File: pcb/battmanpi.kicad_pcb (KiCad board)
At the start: 2 copper layers, 65 x 56 mm, 80 parts, among them CON1 CHARGE PSU, K1 TX2-5V, K2 TX2-5V, P1 SEN+, P2 SEN-, P3 BAT+, P4 BAT-, P5 Raspberry Pi, P6 FAN, Q1 2N3904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

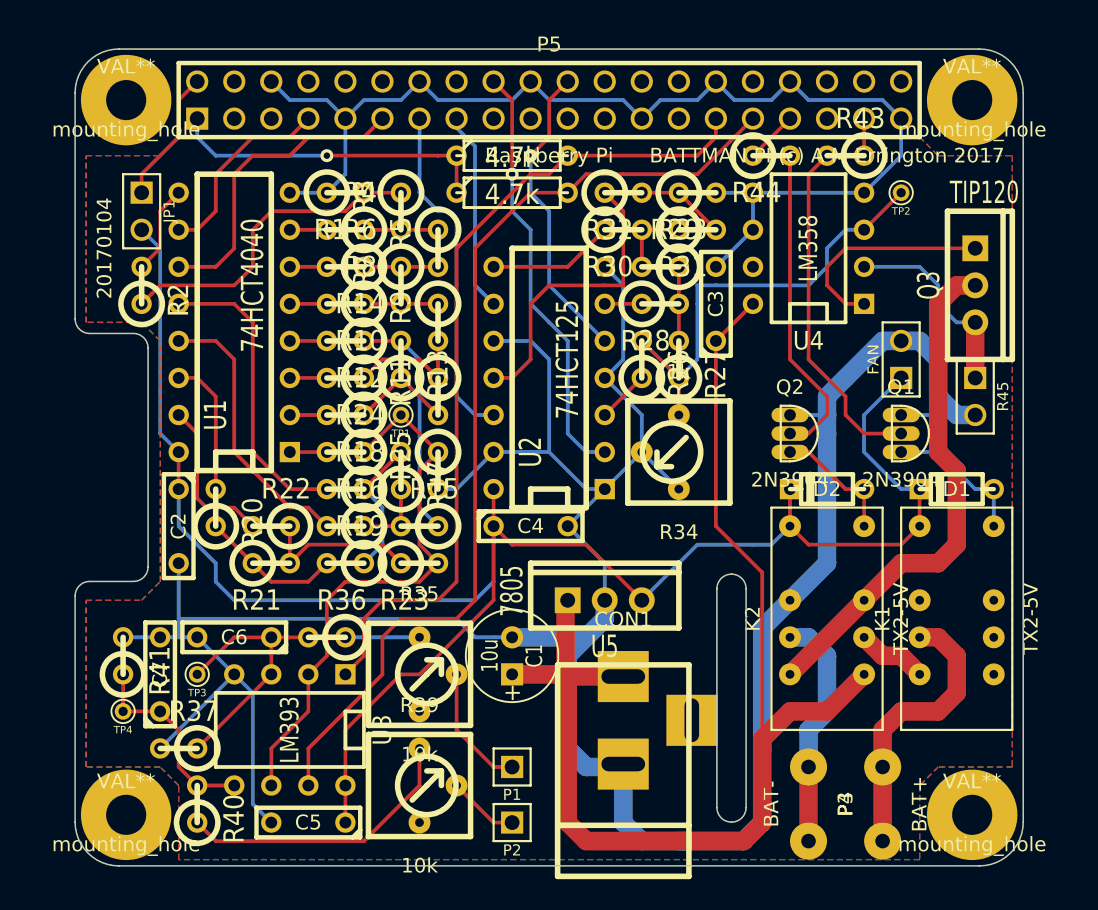
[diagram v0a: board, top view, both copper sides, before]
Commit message: Almost final PCB layout.  All holes set to 0.8 or 1.0 mm (except special components and mounting).  Next make traces slightly wider.
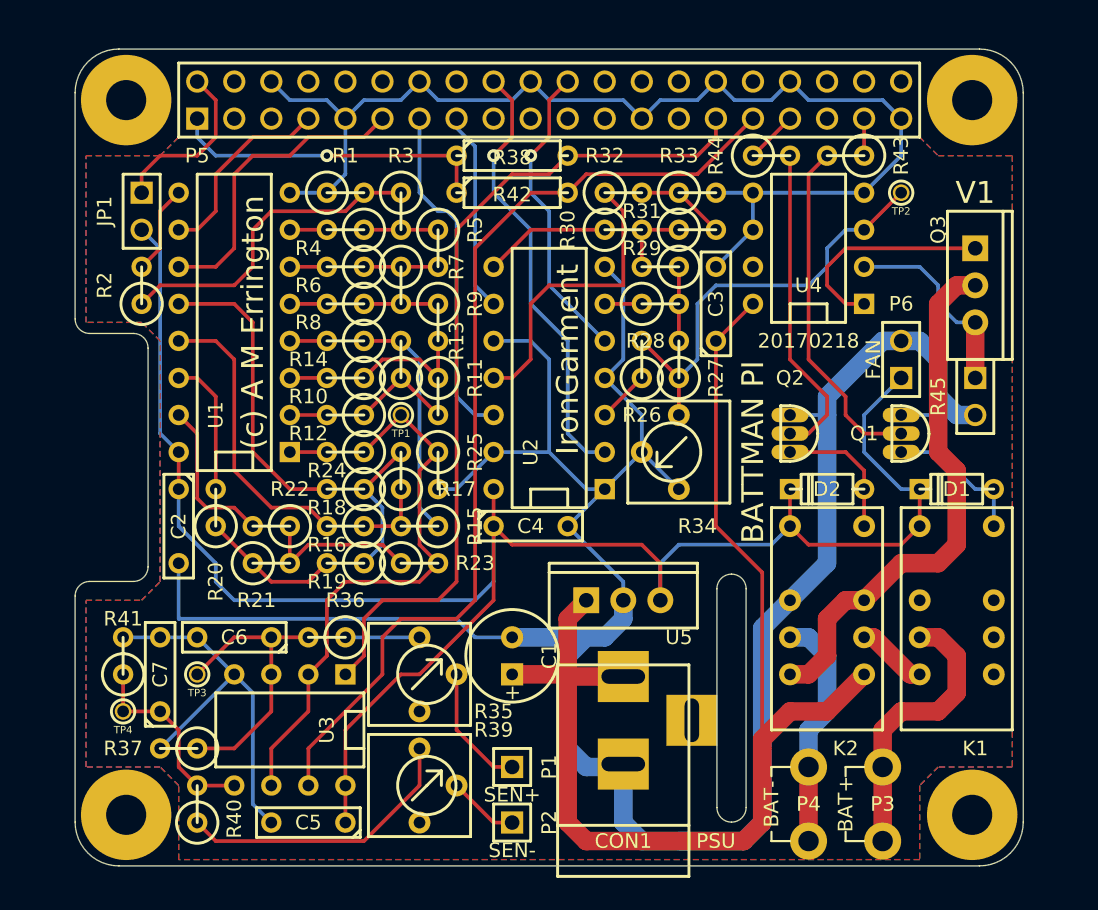
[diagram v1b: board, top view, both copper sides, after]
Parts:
- CON1: value CHARGE PSU -> PSU
- moved U5 1.27 mm to (133.3, 101.6)
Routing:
- net +5V: track 128.5 -> 131.5 mm
- net N-0000067: track 9.20 -> 11.7 mm
- net N-0000032: track 35.2 -> 36.7 mm
- net N-0000030: track 18.4 -> 19.9 mm
- net /D3: track 29.3 -> 30.4 mm
- net /VDAC<B+: track 56.8 -> 57.5 mm
- net N-0000031: track 8.67 -> 9.42 mm
- net N-0000013: track 19.1 -> 19.9 mm
- net N-0000079: track 30.4 -> 29.6 mm
- net +24V: track 84.6 -> 85.1 mm
- net GND: track 281.2 -> 281.8 mm
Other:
- board text added: "(c) A M Errington"
- board text added: "20170218"
- board text added: "BATTMAN PI"
- board text added: "IronGarment"
- board text added: "V1"
- board text removed: "20170104"
- board text removed: "BATTMAN PI (c) A M Errington 2017"

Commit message: Latest KiCad project files
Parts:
- moved R43 14.5 mm to (144.8, 85.1), turned to 270 degrees
- moved R44 14.0 mm to (142.2, 85.1), turned to 270 degrees
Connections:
- P5 pad 13: /D0 -> (no net)
- P5 pad 15: /D1 -> /D0
- P5 pad 16: (no net) -> /D1
- P5 pad 4: (no net) -> N-0000067
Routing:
- net GND: track 281.8 -> 314.5 mm, vias 0 -> 1
- net N-0000030: track 21.9 -> 5.61 mm
- net /CNCT: track 2.54 -> 17.3 mm
- net N-0000027: track 23.7 -> 9.20 mm
- net /MODE: track 3.59 -> 16.3 mm
- net N-0000081: track 15.0 -> 9.20 mm
- net +5V: track 131.5 -> 135.1 mm
- net /D1: track 13.8 -> 17.3 mm
- net /ZERO: track 21.2 -> 18.2 mm
- net N-0000067: track 11.7 -> 13.5 mm
- net /INCR: track 13.5 -> 12.0 mm
- net /D0: track 23.5 -> 22.4 mm
- net /D3: track 30.4 -> 29.3 mm, vias 1 -> 0
- net /D2: track 20.9 -> 19.9 mm, vias 1 -> 0
- net N-000008: track 13.8 -> 14.8 mm
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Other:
- net class hicurrent added: clearance 0.254, trace_width 1.5, via_dia 0.889, via_drill 0.635
- board text added: "20170222"
- board text removed: "20170218"
